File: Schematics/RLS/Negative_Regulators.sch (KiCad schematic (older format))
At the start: 25 parts, among them U4 AD5293, U5 AD5293, U6 LT3015, U7 LT3015

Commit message: Lots of changes
Completed Schematic
1/3 Done PCB
Multisim file for testing ADC protection and buffer circuit
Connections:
- net -V2_ADJ: now reaches R20.1, U4.5 (RB), U6.4 (ADJ)
- net -SDO_SDI: now reaches R19.1, U4.13 (SDO), U5.10 (SDI)
- net -V2_EX_C: now reaches C16.1, U4.7 (EXT_CAP)
- net -V1_ADJ: now reaches R21.1, U5.5 (RB), U7.4 (ADJ)
- net -V1_EX_C: now reaches C15.1, U5.7 (EXT_CAP)
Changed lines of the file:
@@
 LIBS:valves
 LIBS:arduino_shield
-LIBS:arduino_shieldsNCL
+LIBS:RA30421051
+LIBS:RB496EATR
+LIBS:Daughterboard_Connector
 LIBS:RLS-cache
 EELAYER 25 0
@@
 Wire Wire Line
 	3950 2650 3950 2550
+Text Label 5950 2250 1    40   ~ 0
+-V1_ADJ
+Text Label 5950 4900 1    40   ~ 0
+-V2_ADJ
+Text Label 3300 5050 2    40   ~ 0
+-V2_EX_C
+Text Label 3300 2400 2    40   ~ 0
+-V1_EX_C
+Text Label 2950 3500 1    40   ~ 0
+-SDO_SDI
 $EndSCHEMATC

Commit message: Continued PCB and Final Schematic
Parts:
- C10, C12, C14, C4, C6, C8: footprint Capacitors_SMD:C_0603_HandSoldering -> Capacitors_SMD:C_1206_HandSoldering
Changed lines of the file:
@@
 F 0 "C4" H 4425 4150 50  0000 L CNN
 F 1 "0.1uF" H 4425 3950 50  0000 L CNN
-F 2 "Capacitors_SMD:C_0603_HandSoldering" H 4438 3900 50  0001 C CNN
+F 2 "Capacitors_SMD:C_1206_HandSoldering" H 4438 3900 50  0001 C CNN
 F 3 "" H 4400 4050 50  0001 C CNN
 	1    4400 4050
@@
 F 0 "C8" H 3725 4150 50  0000 L CNN
 F 1 "0.1uF" H 3725 3950 50  0000 L CNN
-F 2 "Capacitors_SMD:C_0603_HandSoldering" H 3738 3900 50  0001 C CNN
+F 2 "Capacitors_SMD:C_1206_HandSoldering" H 3738 3900 50  0001 C CNN
 F 3 "" H 3700 4050 50  0001 C CNN
 	1    3700 4050
@@
 F 0 "C10" H 4425 1450 50  0000 L CNN
 F 1 "0.1uF" H 4425 1250 50  0000 L CNN
-F 2 "Capacitors_SMD:C_0603_HandSoldering" H 4438 1200 50  0001 C CNN
+F 2 "Capacitors_SMD:C_1206_HandSoldering" H 4438 1200 50  0001 C CNN
 F 3 "" H 4400 1350 50  0001 C CNN
 	1    4400 1350
@@
 F 0 "C14" H 3725 1450 50  0000 L CNN
 F 1 "0.1uF" H 3725 1250 50  0000 L CNN
-F 2 "Capacitors_SMD:C_0603_HandSoldering" H 3738 1200 50  0001 C CNN
+F 2 "Capacitors_SMD:C_1206_HandSoldering" H 3738 1200 50  0001 C CNN
 F 3 "" H 3700 1350 50  0001 C CNN
 	1    3700 1350
@@
 F 0 "C12" H 4425 2800 50  0000 L CNN
 F 1 "0.1uF" H 4400 2600 50  0000 L CNN
-F 2 "Capacitors_SMD:C_0603_HandSoldering" H 4438 2550 50  0001 C CNN
+F 2 "Capacitors_SMD:C_1206_HandSoldering" H 4438 2550 50  0001 C CNN
 F 3 "" H 4400 2700 50  0001 C CNN
 	1    4400 2700
@@
 F 0 "C6" H 4425 5500 50  0000 L CNN
 F 1 "0.1uF" H 4400 5300 50  0000 L CNN
-F 2 "Capacitors_SMD:C_0603_HandSoldering" H 4438 5250 50  0001 C CNN
+F 2 "Capacitors_SMD:C_1206_HandSoldering" H 4438 5250 50  0001 C CNN
 F 3 "" H 4400 5400 50  0001 C CNN
 	1    4400 5400

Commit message: PCB Layout 90% Done
All that is remaining is the LA traces (moved them and forgot to re-do them) and the SPI and SHDN lines for the digital pots and regs.
Also, do not merge this branch if you can. Have it fully replace the previous folder. There were obsolete files that I removed that Github keeps because it's dumb.
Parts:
- U6, U7: footprint TO_SOT_Packages_THT:TO-220-5_Pentawatt_Multiwatt-5_Vertical_StaggeredType1 -> RLS_CustomFootprints:TO-220-5_Vertical_Type1_w_Heatsink
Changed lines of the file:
@@
 EESchema Schematic File Version 2
-LIBS:RLS-rescue
 LIBS:power
 LIBS:device
@@
 LIBS:contrib
 LIBS:valves
-LIBS:arduino_shield
 LIBS:RA30421051
 LIBS:RB496EATR
@@
 F 0 "U6" H 6150 4750 60  0000 C CNN
 F 1 "LT3015" H 6150 4850 60  0000 C CNN
-F 2 "TO_SOT_Packages_THT:TO-220-5_Pentawatt_Multiwatt-5_Vertical_StaggeredType1" H 6150 4750 60  0001 C CNN
+F 2 "RLS_CustomFootprints:TO-220-5_Vertical_Type1_w_Heatsink" H 6150 4750 60  0001 C CNN
 F 3 "" H 6150 4750 60  0001 C CNN
 	1    6100 4250
@@
 F 0 "U7" H 6150 2100 60  0000 C CNN
 F 1 "LT3015" H 6150 2200 60  0000 C CNN
-F 2 "TO_SOT_Packages_THT:TO-220-5_Pentawatt_Multiwatt-5_Vertical_StaggeredType1" H 6150 2100 60  0001 C CNN
+F 2 "RLS_CustomFootprints:TO-220-5_Vertical_Type1_w_Heatsink" H 6150 2100 60  0001 C CNN
 F 3 "" H 6150 2100 60  0001 C CNN
 	1    6100 1600

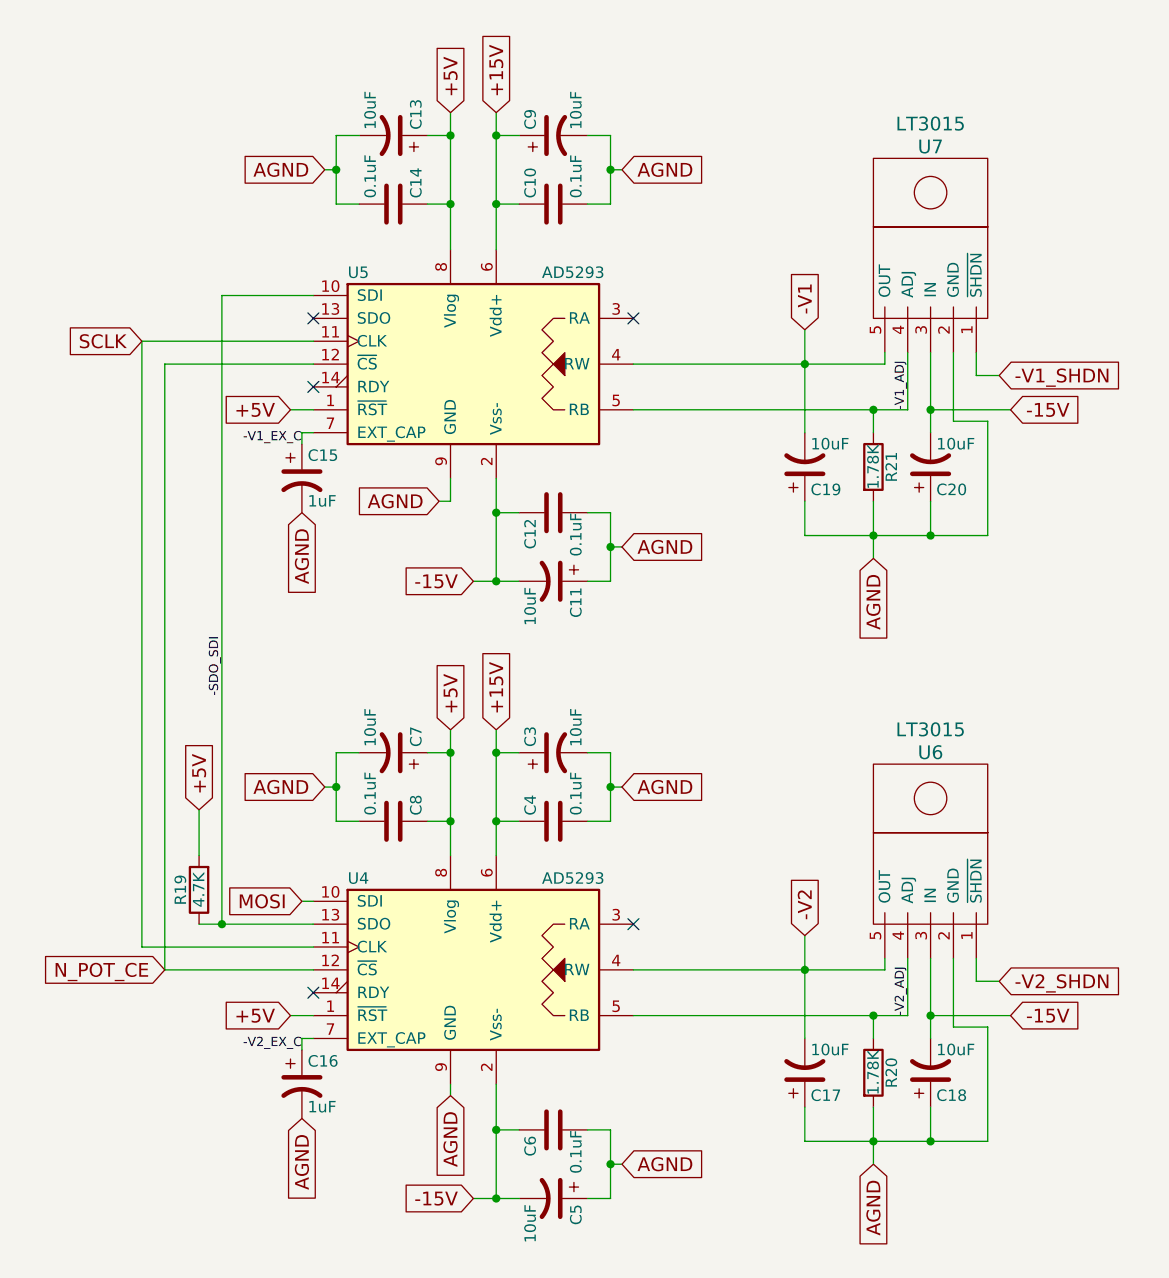
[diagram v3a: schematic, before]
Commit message: Finished PCB but...
Somehow managed to break the schematic file. I know how to fix it, but it is tedious and pointless for now (one has to go through every single individual component and verify that it is the same in the PCB, since the annotation script fucked everything up in the schematic, and therefore any new Netlist).
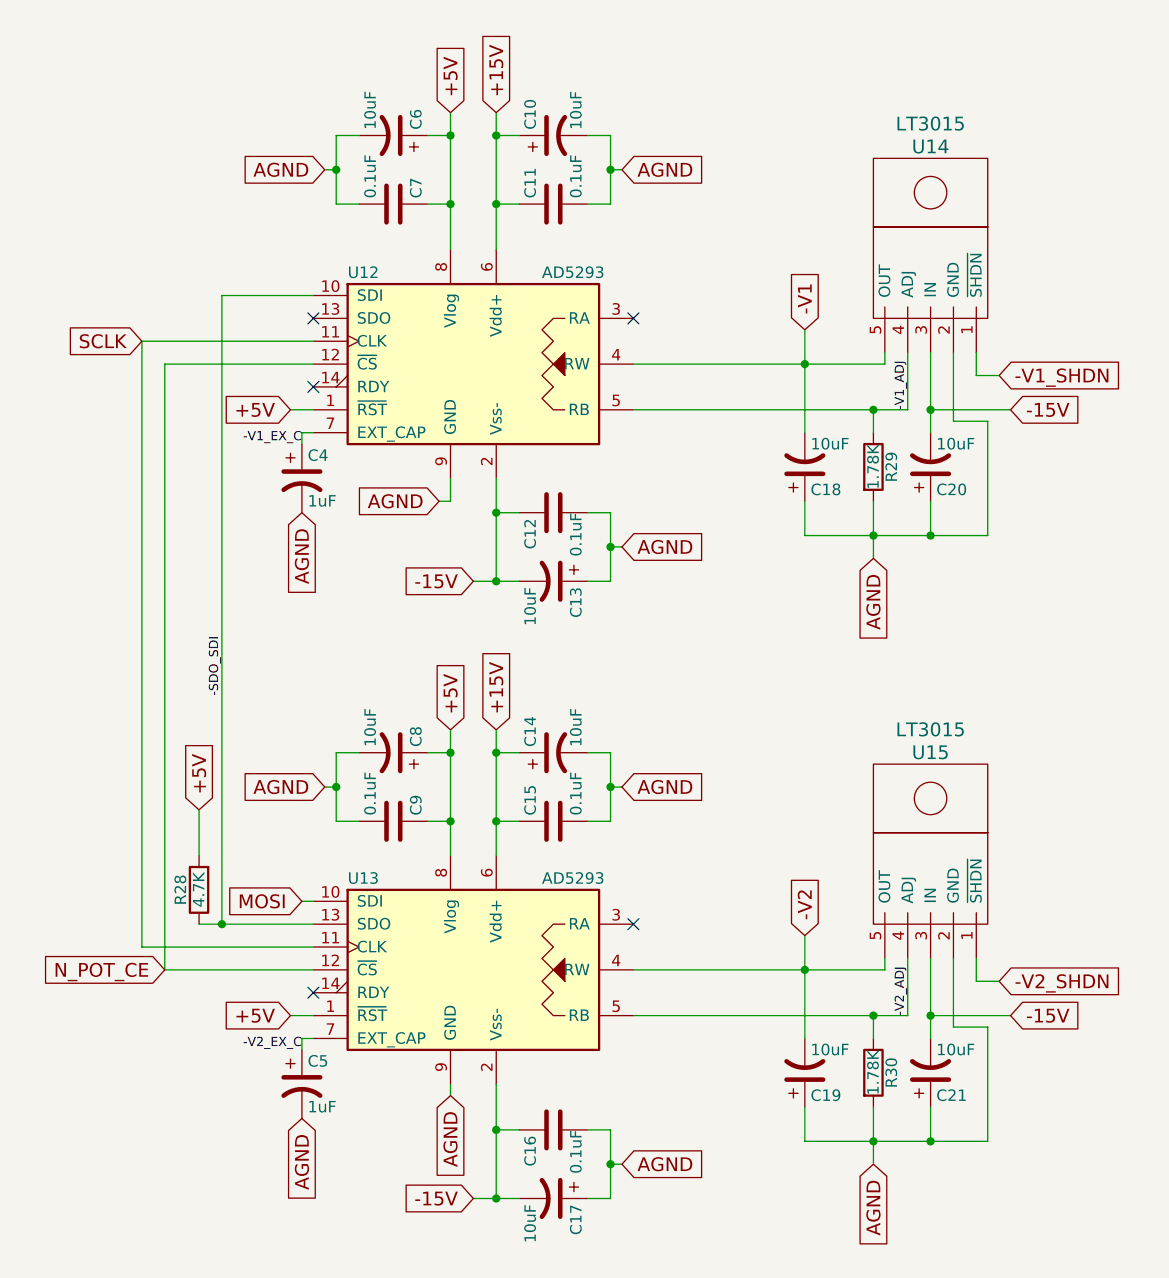
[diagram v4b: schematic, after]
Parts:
- renumbered C9 to C10, C10 to C11, C11 to C13, C3 to C14, C4 to C15, C6 to C16, C5 to C17, C19 to C18, C17 to C19, C18 to C21, C15 to C4, C16 to C5, C13 to C6, C14 to C7, C7 to C8, C8 to C9, R19 to R28, R21 to R29, R20 to R30, U5 to U12, U4 to U13, U7 to U14, U6 to U15
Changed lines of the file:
@@
 $EndDescr
 $Comp
-L LT3015 U6
+L LT3015 U15
 U 1 1 5952FBCC
 P 6100 4250
-F 0 "U6" H 6150 4750 60  0000 C CNN
+F 0 "U15" H 6150 4750 60  0000 C CNN
 F 1 "LT3015" H 6150 4850 60  0000 C CNN
 F 2 "RLS_CustomFootprints:TO-220-5_Vertical_Type1_w_Heatsink" H 6150 4750 60  0001 C CNN
@@
 $EndComp
 $Comp
-L AD5293-RESCUE-RLS U4
+L AD5293-RESCUE-RLS U13
 U 1 1 595305F7
 P 4050 4700
-AR Path="/595305F7" Ref="U4"  Part="1"
-AR Path="/5952F710/595305F7" Ref="U4"  Part="1"
-F 0 "U4" H 3500 5100 50  0000 L CNN
+F 0 "U13" H 3500 5100 50  0000 L CNN
 F 1 "AD5293" H 4350 5100 50  0000 L CNN
 F 2 "SMD_Packages:SSOP-14" H 4050 4700 50  0001 C CNN
@@
 $EndComp
 $Comp
-L AD5293-RESCUE-RLS U5
+L AD5293-RESCUE-RLS U12
 U 1 1 59530648
 P 4050 2050
-AR Path="/59530648" Ref="U5"  Part="1"
-AR Path="/5952F710/59530648" Ref="U5"  Part="1"
-F 0 "U5" H 3500 2450 50  0000 L CNN
+F 0 "U12" H 3500 2450 50  0000 L CNN
 F 1 "AD5293" H 4350 2450 50  0000 L CNN
 F 2 "SMD_Packages:SSOP-14" H 4050 2050 50  0001 C CNN
@@
 $EndComp
 $Comp
-L CP1 C15
+L CP1 C4
 U 1 1 59582C1E
 P 3300 2550
-F 0 "C15" H 3325 2650 50  0000 L CNN
+F 0 "C4" H 3325 2650 50  0000 L CNN
 F 1 "1uF" H 3325 2450 50  0000 L CNN
 F 2 "Capacitors_SMD:CP_Elec_4x5.3" H 3300 2550 50  0001 C CNN
@@
 $EndComp
 $Comp
-L CP1 C16
+L CP1 C5
 U 1 1 59582C25
 P 3300 5200
-F 0 "C16" H 3325 5300 50  0000 L CNN
+F 0 "C5" H 3325 5300 50  0000 L CNN
 F 1 "1uF" H 3325 5100 50  0000 L CNN
 F 2 "Capacitors_SMD:CP_Elec_4x5.3" H 3300 5200 50  0001 C CNN
@@
 $EndComp
 $Comp
-L CP1 C3
+L CP1 C14
 U 1 1 59582C2C
 P 4400 3750
-F 0 "C3" H 4425 3850 50  0000 L CNN
+F 0 "C14" H 4425 3850 50  0000 L CNN
 F 1 "10uF" H 4425 3650 50  0000 L CNN
 F 2 "Capacitors_SMD:CP_Elec_4x5.3" H 4400 3750 50  0001 C CNN
@@
 $EndComp
 $Comp
-L C C4
+L C C15
 U 1 1 5958315B
 P 4400 4050
-F 0 "C4" H 4425 4150 50  0000 L CNN
+F 0 "C15" H 4425 4150 50  0000 L CNN
 F 1 "0.1uF" H 4425 3950 50  0000 L CNN
 F 2 "Capacitors_SMD:C_1206_HandSoldering" H 4438 3900 50  0001 C CNN
@@
 $EndComp
 $Comp
-L R R19
+L R R28
 U 1 1 5958317D
 P 2850 4350
-F 0 "R19" V 2930 4350 50  0000 C CNN
+F 0 "R28" V 2930 4350 50  0000 C CNN
 F 1 "4.7K" V 2850 4350 50  0000 C CNN
 F 2 "Resistors_SMD:R_0805_HandSoldering" V 2780 4350 50  0001 C CNN
@@
 $EndComp
 $Comp
-L CP1 C7
+L CP1 C8
 U 1 1 5958F709
 P 3700 3750
-F 0 "C7" H 3725 3850 50  0000 L CNN
+F 0 "C8" H 3725 3850 50  0000 L CNN
 F 1 "10uF" H 3725 3650 50  0000 L CNN
 F 2 "Capacitors_SMD:CP_Elec_4x5.3" H 3700 3750 50  0001 C CNN
@@
 $EndComp
 $Comp
-L C C8
+L C C9
 U 1 1 5958F710
 P 3700 4050
-F 0 "C8" H 3725 4150 50  0000 L CNN
+F 0 "C9" H 3725 4150 50  0000 L CNN
 F 1 "0.1uF" H 3725 3950 50  0000 L CNN
 F 2 "Capacitors_SMD:C_1206_HandSoldering" H 3738 3900 50  0001 C CNN
@@
 AGND
 $Comp
-L CP1 C9
+L CP1 C10
 U 1 1 59590FE8
 P 4400 1050
-F 0 "C9" H 4425 1150 50  0000 L CNN
+F 0 "C10" H 4425 1150 50  0000 L CNN
 F 1 "10uF" H 4425 950 50  0000 L CNN
 F 2 "Capacitors_SMD:CP_Elec_4x5.3" H 4400 1050 50  0001 C CNN
@@
 $EndComp
 $Comp
-L C C10
+L C C11
 U 1 1 59590FEF
 P 4400 1350
-F 0 "C10" H 4425 1450 50  0000 L CNN
+F 0 "C11" H 4425 1450 50  0000 L CNN
 F 1 "0.1uF" H 4425 1250 50  0000 L CNN
 F 2 "Capacitors_SMD:C_1206_HandSoldering" H 4438 1200 50  0001 C CNN
@@
 $EndComp
 $Comp
-L CP1 C13
+L CP1 C6
 U 1 1 59590FF6
 P 3700 1050
-F 0 "C13" H 3725 1150 50  0000 L CNN
+F 0 "C6" H 3725 1150 50  0000 L CNN
 F 1 "10uF" H 3725 950 50  0000 L CNN
 F 2 "Capacitors_SMD:CP_Elec_4x5.3" H 3700 1050 50  0001 C CNN
@@
 $EndComp
 $Comp
-L C C14
+L C C7
 U 1 1 59590FFD
 P 3700 1350
-F 0 "C14" H 3725 1450 50  0000 L CNN
+F 0 "C7" H 3725 1450 50  0000 L CNN
 F 1 "0.1uF" H 3725 1250 50  0000 L CNN
 F 2 "Capacitors_SMD:C_1206_HandSoldering" H 3738 1200 50  0001 C CNN
@@
 AGND
 $Comp
-L CP1 C11
+L CP1 C13
 U 1 1 59593FD8
 P 4400 3000
-F 0 "C11" H 4425 3100 50  0000 L CNN
+F 0 "C13" H 4425 3100 50  0000 L CNN
 F 1 "10uF" H 4425 2900 50  0000 L CNN
 F 2 "Capacitors_SMD:CP_Elec_4x5.3" H 4400 3000 50  0001 C CNN
@@
 -15V
 $Comp
-L CP1 C5
+L CP1 C17
 U 1 1 59594AB0
 P 4400 5700
-F 0 "C5" H 4425 5800 50  0000 L CNN
+F 0 "C17" H 4425 5800 50  0000 L CNN
 F 1 "10uF" H 4425 5600 50  0000 L CNN
 F 2 "Capacitors_SMD:CP_Elec_4x5.3" H 4400 5700 50  0001 C CNN
@@
 $EndComp
 $Comp
-L C C6
+L C C16
 U 1 1 59594AB7
 P 4400 5400
-F 0 "C6" H 4425 5500 50  0000 L CNN
+F 0 "C16" H 4425 5500 50  0000 L CNN
 F 1 "0.1uF" H 4400 5300 50  0000 L CNN
 F 2 "Capacitors_SMD:C_1206_HandSoldering" H 4438 5250 50  0001 C CNN
@@
 AGND
 $Comp
-L R R20
+L R R30
 U 1 1 5959FDF4
 P 5800 5150
-F 0 "R20" V 5880 5150 50  0000 C CNN
+F 0 "R30" V 5880 5150 50  0000 C CNN
 F 1 "1.78K" V 5800 5150 50  0000 C CNN
 F 2 "Resistors_SMD:R_1206_HandSoldering" V 5730 5150 50  0001 C CNN
@@
 $EndComp
 $Comp
-L CP1 C17
+L CP1 C19
 U 1 1 5959FE9D
 P 5500 5150
-F 0 "C17" H 5525 5250 50  0000 L CNN
+F 0 "C19" H 5525 5250 50  0000 L CNN
 F 1 "10uF" H 5525 5050 50  0000 L CNN
 F 2 "Capacitors_SMD:CP_Elec_4x5.3" H 5500 5150 50  0001 C CNN
@@
 $EndComp
 $Comp
-L CP1 C18
+L CP1 C21
 U 1 1 5959FFA5
 P 6050 5150
-F 0 "C18" H 6075 5250 50  0000 L CNN
+F 0 "C21" H 6075 5250 50  0000 L CNN
 F 1 "10uF" H 6075 5050 50  0000 L CNN
 F 2 "Capacitors_SMD:CP_Elec_4x5.3" H 6050 5150 50  0001 C CNN
@@
 -V2
 $Comp
-L LT3015 U7
+L LT3015 U14
 U 1 1 595A20C2
 P 6100 1600
-F 0 "U7" H 6150 2100 60  0000 C CNN
+F 0 "U14" H 6150 2100 60  0000 C CNN
 F 1 "LT3015" H 6150 2200 60  0000 C CNN
 F 2 "RLS_CustomFootprints:TO-220-5_Vertical_Type1_w_Heatsink" H 6150 2100 60  0001 C CNN
@@
 $EndComp
 $Comp
-L R R21
+L R R29
 U 1 1 595A20CD
 P 5800 2500
-F 0 "R21" V 5880 2500 50  0000 C CNN
+F 0 "R29" V 5880 2500 50  0000 C CNN
 F 1 "1.78K" V 5800 2500 50  0000 C CNN
 F 2 "Resistors_SMD:R_1206_HandSoldering" V 5730 2500 50  0001 C CNN
@@
 $EndComp
 $Comp
-L CP1 C19
+L CP1 C18
 U 1 1 595A20D4
 P 5500 2500
-F 0 "C19" H 5525 2600 50  0000 L CNN
+F 0 "C18" H 5525 2600 50  0000 L CNN
 F 1 "10uF" H 5525 2400 50  0000 L CNN
 F 2 "Capacitors_SMD:CP_Elec_4x5.3" H 5500 2500 50  0001 C CNN

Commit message: MAJOR CHANGE! READ BELOW
Due to layout issues, I changed the pins used for the variable regulator shutdown lines. +V1_SHDN is now AA9, +V2_SHDN is now AA8, -V1_SHDN is now AA11, and -V2_SHDN is now AA10. MAKE SURE TO CHANGE THE RESPECTIVE CODE (Paolo).

Included in this upload is the pre-design review finish PCB and Schematic, with pdf files of each for printing and easy reference.
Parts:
- U12, U13: footprint SMD_Packages:SSOP-14 -> Housings_SSOP:TSSOP-14_4.4x5mm_Pitch0.65mm
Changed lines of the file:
@@
 Sheet 4 7
 Title "Remote Lab System"
-Date ""
-Rev ""
-Comp ""
+Date "2017-07-18"
+Rev "15"
+Comp "University of Washington, Bothell"
 Comment1 ""
 Comment2 ""
@@
 F 0 "U13" H 3500 5100 50  0000 L CNN
 F 1 "AD5293" H 4350 5100 50  0000 L CNN
-F 2 "SMD_Packages:SSOP-14" H 4050 4700 50  0001 C CNN
+F 2 "Housings_SSOP:TSSOP-14_4.4x5mm_Pitch0.65mm" H 4050 4700 50  0001 C CNN
 F 3 "" H 4050 4700 50  0001 C CNN
 	1    4050 4700
@@
 F 0 "U12" H 3500 2450 50  0000 L CNN
 F 1 "AD5293" H 4350 2450 50  0000 L CNN
-F 2 "SMD_Packages:SSOP-14" H 4050 2050 50  0001 C CNN
+F 2 "Housings_SSOP:TSSOP-14_4.4x5mm_Pitch0.65mm" H 4050 2050 50  0001 C CNN
 F 3 "" H 4050 2050 50  0001 C CNN
 	1    4050 2050
